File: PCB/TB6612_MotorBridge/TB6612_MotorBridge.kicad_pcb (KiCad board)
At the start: 4 copper layers, 44 x 44 mm, 14 parts, among them J1 Conn_01x07, J2 Conn_01x07, J3 Screw_Terminal_01x02, J4 Conn_01x06, J5 Conn_01x06, U1 TB6612FNG, U2 DMG3415U-7

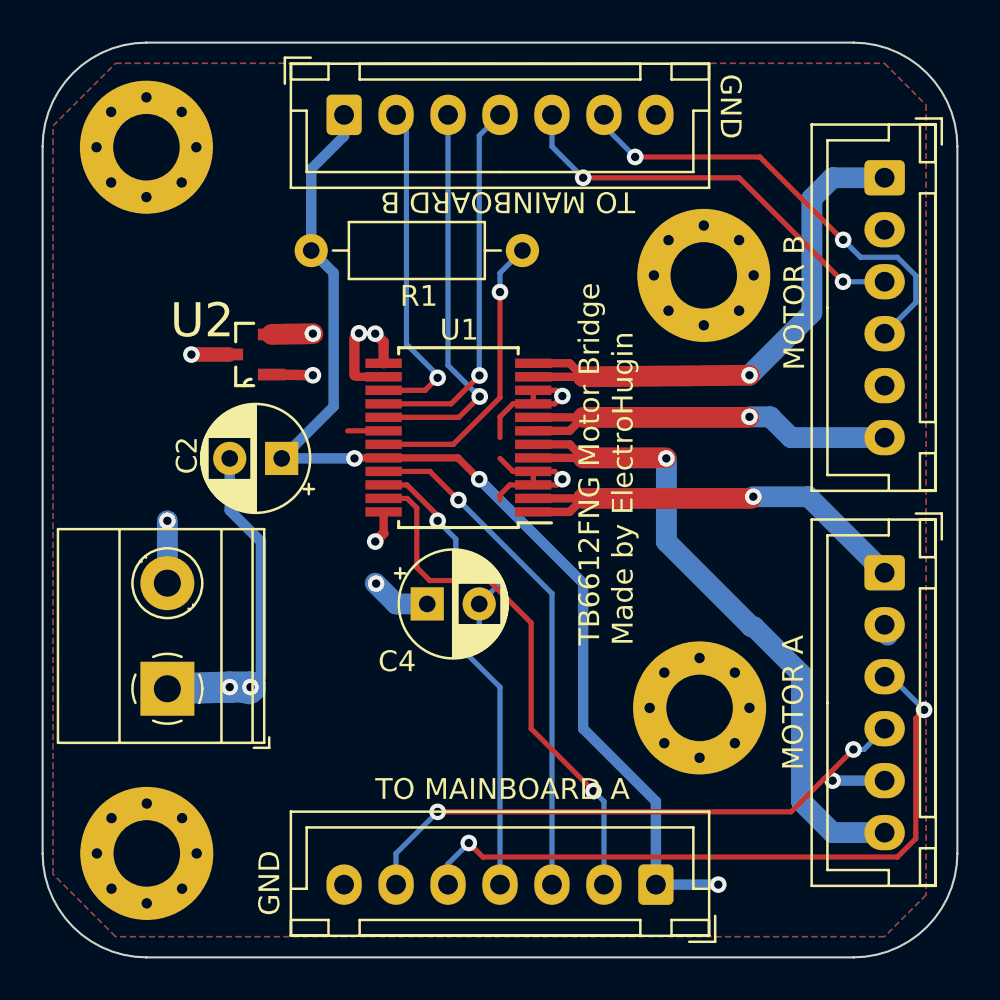
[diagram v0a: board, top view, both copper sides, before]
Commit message: Converted all vias to through-hole
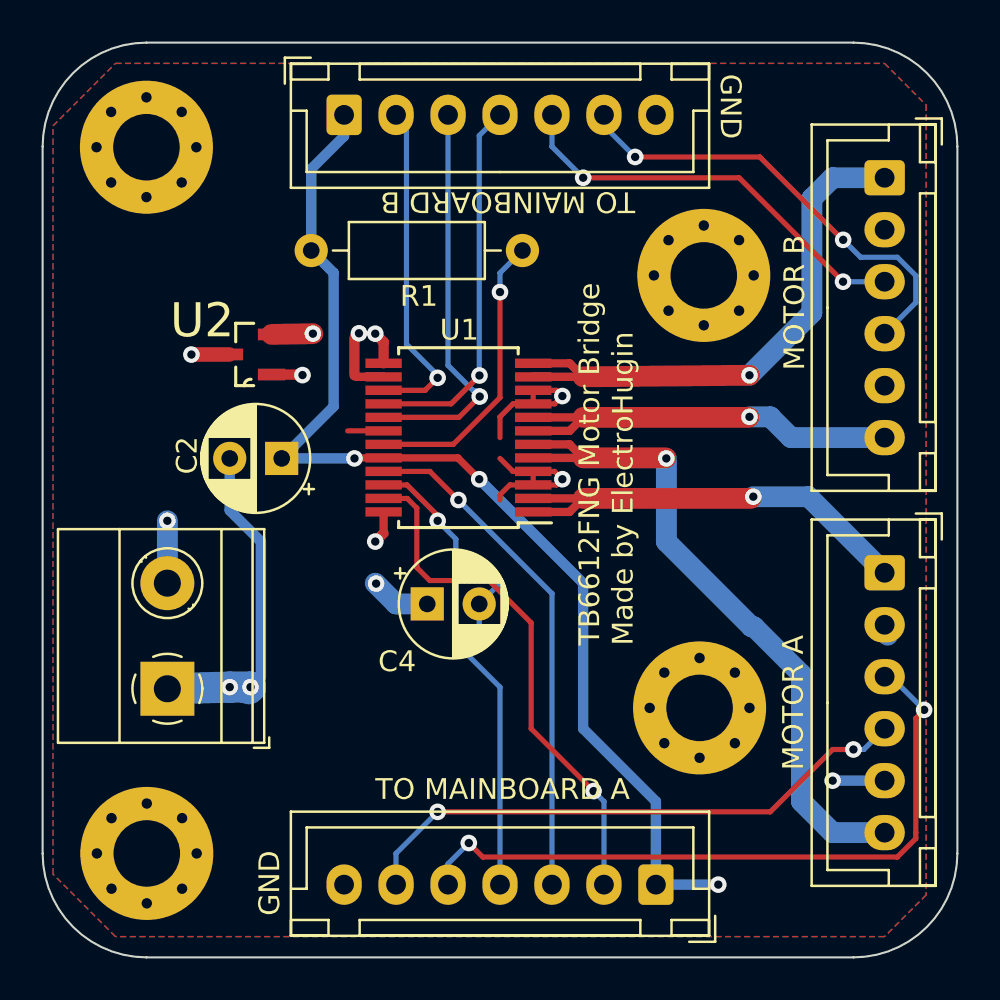
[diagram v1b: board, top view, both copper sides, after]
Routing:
- net GND: track 37.5 -> 37.0 mm
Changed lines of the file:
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@@
     (fp_line (start 17.45 3.4) (end 17.45 -2.35)
       (stroke (width 0.1) (type solid)) (layer "F.Fab"))
-    (pad "1" thru_hole roundrect (at 0 0) (size 1.7 1.95) (drill 0.95) (layers "*.Cu" "*.Mask") (roundrect_rratio 0.147059)
+    (pad "1" thru_hole roundrect (at 0 0) (size 1.7 1.95) (drill 0.95) (layers "*.Cu" "*.Mask") (roundrect_rratio 0.1470588235)
       (net 1 "+3.3V") (pinfunction "Pin_1") (pintype "passive"))
     (pad "2" thru_hole oval (at 2.5 0) (size 1.7 1.95) (drill 0.95) (layers "*.Cu" "*.Mask")
@@
     (fp_line (start 14.95 3.4) (end 14.95 -2.35)
       (stroke (width 0.1) (type solid)) (layer "F.Fab"))
-    (pad "1" thru_hole roundrect (at 0 0 270) (size 1.7 1.95) (drill 0.95) (layers "*.Cu" "*.Mask") (roundrect_rratio 0.147059)
+    (pad "1" thru_hole roundrect (at 0 0 270) (size 1.7 1.95) (drill 0.95) (layers "*.Cu" "*.Mask") (roundrect_rratio 0.1470588235)
       (net 12 "/MB1") (pinfunction "Pin_1") (pintype "passive"))
     (pad "2" thru_hole oval (at 2.5 0 270) (size 1.7 1.95) (drill 0.95) (layers "*.Cu" "*.Mask")
@@
     (fp_line (start 14.95 3.4) (end 14.95 -2.35)
       (stroke (width 0.1) (type solid)) (layer "F.Fab"))
-    (pad "1" thru_hole roundrect (at 0 0 270) (size 1.7 1.95) (drill 0.95) (layers "*.Cu" "*.Mask") (roundrect_rratio 0.147059)
+    (pad "1" thru_hole roundrect (at 0 0 270) (size 1.7 1.95) (drill 0.95) (layers "*.Cu" "*.Mask") (roundrect_rratio 0.1470588235)
       (net 10 "/MA1") (pinfunction "Pin_1") (pintype "passive"))
     (pad "2" thru_hole oval (at 2.5 0 270) (size 1.7 1.95) (drill 0.95) (layers "*.Cu" "*.Mask")
@@
     (fp_line (start 17.45 3.4) (end 17.45 -2.35)
       (stroke (width 0.1) (type solid)) (layer "F.Fab"))
-    (pad "1" thru_hole roundrect (at 0 0 180) (size 1.7 1.95) (drill 0.95) (layers "*.Cu" "*.Mask") (roundrect_rratio 0.147059)
+    (pad "1" thru_hole roundrect (at 0 0 180) (size 1.7 1.95) (drill 0.95) (layers "*.Cu" "*.Mask") (roundrect_rratio 0.1470588235)
       (net 1 "+3.3V") (pinfunction "Pin_1") (pintype "passive"))
     (pad "2" thru_hole oval (at 2.5 0 180) (size 1.7 1.95) (drill 0.95) (layers "*.Cu" "*.Mask")
@@
   (segment (start 130.025 86.975) (end 130 87) (width 0.25) (layer "F.Cu") (net 1))
   (segment (start 136 88) (end 134.975 86.975) (width 0.35) (layer "F.Cu") (net 1))
+  (via (at 147.5 107.5) (size 0.8) (drill 0.4) (layers "F.Cu" "B.Cu") (net 1))
   (via (at 130 87) (size 0.8) (drill 0.4) (layers "F.Cu" "B.Cu") (net 1))
+  (via (at 153 102.5) (size 0.8) (drill 0.4) (layers "F.Cu" "B.Cu") (net 1))
   (via (at 136 88) (size 0.8) (drill 0.4) (layers "F.Cu" "B.Cu") (net 1))
   (segment (start 154 83.5) (end 155.5 83.5) (width 0.5) (layer "In2.Cu") (net 1))
@@
   (segment (start 153 84.5) (end 154 83.5) (width 0.5) (layer "In2.Cu") (net 1))
   (segment (start 152.5 102.5) (end 147.5 107.5) (width 0.5) (layer "In2.Cu") (net 1))
-  (via blind (at 147.5 107.5) (size 0.8) (drill 0.4) (layers "In2.Cu" "B.Cu") (net 1))
-  (via blind (at 153 102.5) (size 0.8) (drill 0.4) (layers "In2.Cu" "B.Cu") (net 1))
   (segment (start 129.5 71.5) (end 127.92 73.08) (width 0.5) (layer "B.Cu") (net 1))
   (segment (start 144.5 107.5) (end 147.5 107.5) (width 0.5) (layer "B.Cu") (net 1))
@@
   (segment (start 137.625 87.625) (end 138.6 87.625) (width 0.25) (layer "F.Cu") (net 2))
   (segment (start 138.6 88.275) (end 137.475 88.275) (width 0.25) (layer "F.Cu") (net 2))
-  (segment (start 126.016 82.9652) (end 128 83) (width 0.5) (layer "F.Cu") (net 2))
   (segment (start 139.725 88.275) (end 138.6 88.275) (width 0.25) (layer "F.Cu") (net 2))
   (segment (start 137.625 84.375) (end 137 85) (width 0.25) (layer "F.Cu") (net 2))
+  (segment (start 127.47397 82.9652) (end 127.5 82.99123) (width 0.5) (layer "F.Cu") (net 2))
   (segment (start 139.625 87.625) (end 140 88) (width 0.25) (layer "F.Cu") (net 2))
   (segment (start 138.6 83.725) (end 139.725 83.725) (width 0.25) (layer "F.Cu") (net 2))
@@
   (segment (start 138.6 84.375) (end 138.6 83.725) (width 0.25) (layer "F.Cu") (net 2))
   (segment (start 137.625 87.625) (end 137 87) (width 0.25) (layer "F.Cu") (net 2))
+  (segment (start 126.016 82.9652) (end 127.47397 82.9652) (width 0.5) (layer "F.Cu") (net 2))
   (segment (start 138.6 87.625) (end 139.625 87.625) (width 0.25) (layer "F.Cu") (net 2))
   (segment (start 140 84) (end 139.625 84.375) (width 0.25) (layer "F.Cu") (net 2))
   (segment (start 137 85) (end 137 86) (width 0.25) (layer "F.Cu") (net 2))
-  (segment (start 128 83) (end 127.9652 82.9652) (width 0.5) (layer "F.Cu") (net 2))
-  (via blind (at 128 83) (size 0.8) (drill 0.4) (layers "F.Cu" "In1.Cu") (net 2))
-  (via blind (at 140 88) (size 0.8) (drill 0.4) (layers "F.Cu" "In1.Cu") (net 2))
-  (via blind (at 140 84) (size 0.8) (drill 0.4) (layers "F.Cu" "In1.Cu") (net 2))
-  (via blind (at 124 98) (size 0.8) (drill 0.4) (layers "In1.Cu" "B.Cu") (net 2))
-  (via blind (at 125 98) (size 0.8) (drill 0.4) (layers "In1.Cu" "B.Cu") (net 2))
+  (via (at 127.5 82.99123) (size 0.8) (drill 0.4) (layers "F.Cu" "B.Cu") (net 2))
+  (via (at 124 98) (size 0.8) (drill 0.4) (layers "F.Cu" "B.Cu") (net 2))
+  (via (at 140 88) (size 0.8) (drill 0.4) (layers "F.Cu" "B.Cu") (net 2))
+  (via (at 140 84) (size 0.8) (drill 0.4) (layers "F.Cu" "B.Cu") (net 2))
+  (via (at 125 98) (size 0.8) (drill 0.4) (layers "F.Cu" "B.Cu") (net 2))
   (segment (start 124 98) (end 125 98) (width 1.5) (layer "B.Cu") (net 2))
   (segment (start 136 94) (end 136 95) (width 0.25) (layer "B.Cu") (net 2))
@@
   (via (at 128 81) (size 0.8) (drill 0.4) (layers "F.Cu" "B.Cu") (net 3))
   (via (at 131.041638 93.020819) (size 0.8) (drill 0.4) (layers "F.Cu" "B.Cu") (net 3))
-  (segment (start 128 88) (end 131 91) (width 1) (layer "In2.Cu") (net 3))
   (segment (start 128 81) (end 129 81) (width 1) (layer "In2.Cu") (net 3))
   (segment (start 131.041638 93.020819) (end 131.041638 91.041638) (width 1) (layer "In2.Cu") (net 3))
-  (segment (start 129 81) (end 129 85) (width 1) (layer "In2.Cu") (net 3))
+  (segment (start 128 88) (end 131 91) (width 1) (layer "In2.Cu") (net 3))
+  (segment (start 131.041638 91.041638) (end 131 91) (width 0.25) (layer "In2.Cu") (net 3))
   (segment (start 129 85) (end 128 86) (width 1) (layer "In2.Cu") (net 3))
   (segment (start 128 86) (end 128 88) (width 1) (layer "In2.Cu") (net 3))
-  (segment (start 131.041638 91.041638) (end 131 91) (width 0.25) (layer "In2.Cu") (net 3))
+  (segment (start 129 81) (end 129 85) (width 1) (layer "In2.Cu") (net 3))
   (segment (start 129 81) (end 131 81) (width 1) (layer "In2.Cu") (net 3))
   (segment (start 133.5 94) (end 132 94) (width 1) (layer "B.Cu") (net 3))
@@
   (segment (start 122.160263 82) (end 122.156142 82.004121) (width 0.25) (layer "F.Cu") (net 15))
   (segment (start 123.984 82) (end 122.160263 82) (width 0.7) (layer "F.Cu") (net 15))
-  (via blind (at 122.156142 82.004121) (size 0.8) (drill 0.4) (layers "F.Cu" "In2.Cu") (net 15))
+  (via (at 121 90) (size 0.8) (drill 0.4) (layers "F.Cu" "B.Cu") (net 15))
+  (via (at 122.156142 82.004121) (size 0.8) (drill 0.4) (layers "F.Cu" "B.Cu") (net 15))
   (segment (start 121 83) (end 122 82) (width 1) (layer "In2.Cu") (net 15))
   (segment (start 121 90) (end 121 83) (width 1) (layer "In2.Cu") (net 15))
-  (via blind (at 121 90) (size 0.8) (drill 0.4) (layers "In2.Cu" "B.Cu") (net 15))
   (segment (start 121 93) (end 121 90) (width 1) (layer "B.Cu") (net 15))
   (segment (start 157 99.5) (end 157.5 99) (width 0.25) (layer "F.Cu") (net 16))
@@
   (segment (start 155.805807 97.5) (end 155.5 97.5) (width 0.25) (layer "B.Cu") (net 16))
   (segment (start 134.5 106.5) (end 135.5 105.5) (width 0.25) (layer "B.Cu") (net 16))
-  (segment (start 134 104) (end 151 104) (width 0.25) (layer "F.Cu") (net 17))
-  (segment (start 151 104) (end 154 101) (width 0.25) (layer "F.Cu") (net 17))
+  (segment (start 153 101) (end 154 101) (width 0.25) (layer "F.Cu") (net 17))
+  (segment (start 150 104) (end 153 101) (width 0.25) (layer "F.Cu") (net 17))
+  (segment (start 134 104) (end 150 104) (width 0.25) (layer "F.Cu") (net 17))
   (via (at 134 104) (size 0.8) (drill 0.4) (layers "F.Cu" "B.Cu") (net 17))
   (via (at 154 101) (size 0.8) (drill 0.4) (layers "F.Cu" "B.Cu") (net 17))

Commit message: Added Visuals
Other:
- board text added: "12V"
- board text added: "JLCJLCJLCJLC"
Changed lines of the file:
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@@
+    (effects (font (size 1 1) (thickness 0.15)) (justify left bottom))
+  )
+  (gr_text "12V" (at 127.227798 94.336136 90) (layer "F.SilkS")
+    (effects (font (size 1 1) (thickness 0.15)) (justify left bottom))
+  )
+  (gr_text "GND" (at 127.227798 99.527583 90) (layer "F.SilkS")
     (effects (font (size 1 1) (thickness 0.15)) (justify left bottom))
   )
@@
     (effects (font (size 1 1) (thickness 0.15)) (justify left bottom))
   )
+  (gr_text "JLCJLCJLCJLC" (at 130.170032 73.174071) (layer "F.SilkS")
+    (effects (font (size 1 1) (thickness 0.15)) (justify left bottom))
+  )
